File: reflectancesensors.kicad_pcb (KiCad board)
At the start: 2 copper layers, 42 x 29.5 mm, 10 parts, among them J1 Power, J2 Outputs, U1 TCRT5000L, U3 TCRT5000L

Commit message: some small changes
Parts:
- added H1: MountingHole, MountingHole:MountingHole_3.2mm_M3_DIN965, F.Cu at (79.0, 96.0)
- added H2: MountingHole, MountingHole:MountingHole_3.2mm_M3_DIN965, F.Cu at (79.0, 103.2)
- added H3: MountingHole, MountingHole:MountingHole_3.2mm_M3_DIN965, F.Cu at (79.0, 110.3)
- added H4: MountingHole, MountingHole:MountingHole_3.2mm_M3_DIN965, F.Cu at (79.0, 117.5)
- GND +3V3: renamed from J1
- Outputs 1,2: renamed from J2
- renumbered U3 to U1, U1 to U2
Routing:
- net GND: vias 90 -> 100
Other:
- board size 42 x 29.5 mm -> 48.5 x 35.5 mm

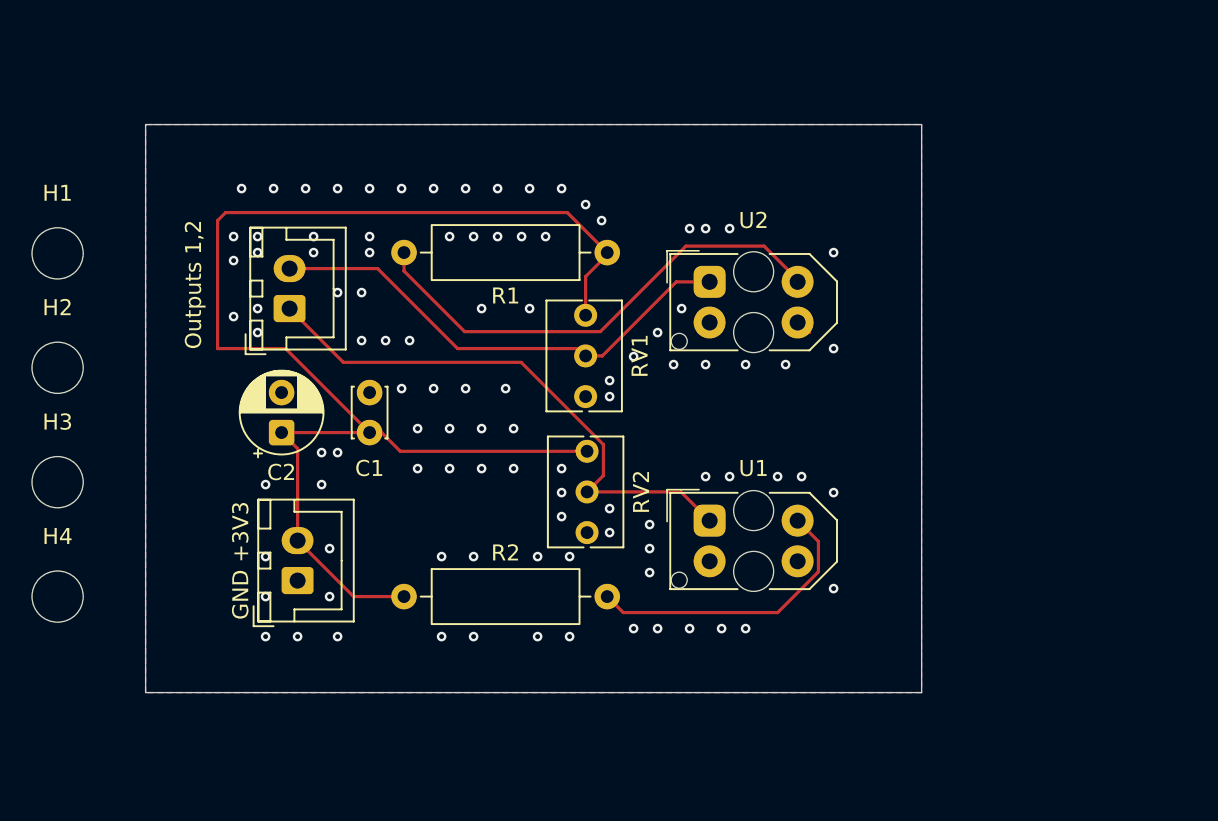
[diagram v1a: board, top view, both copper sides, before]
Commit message: adding high power reflectance
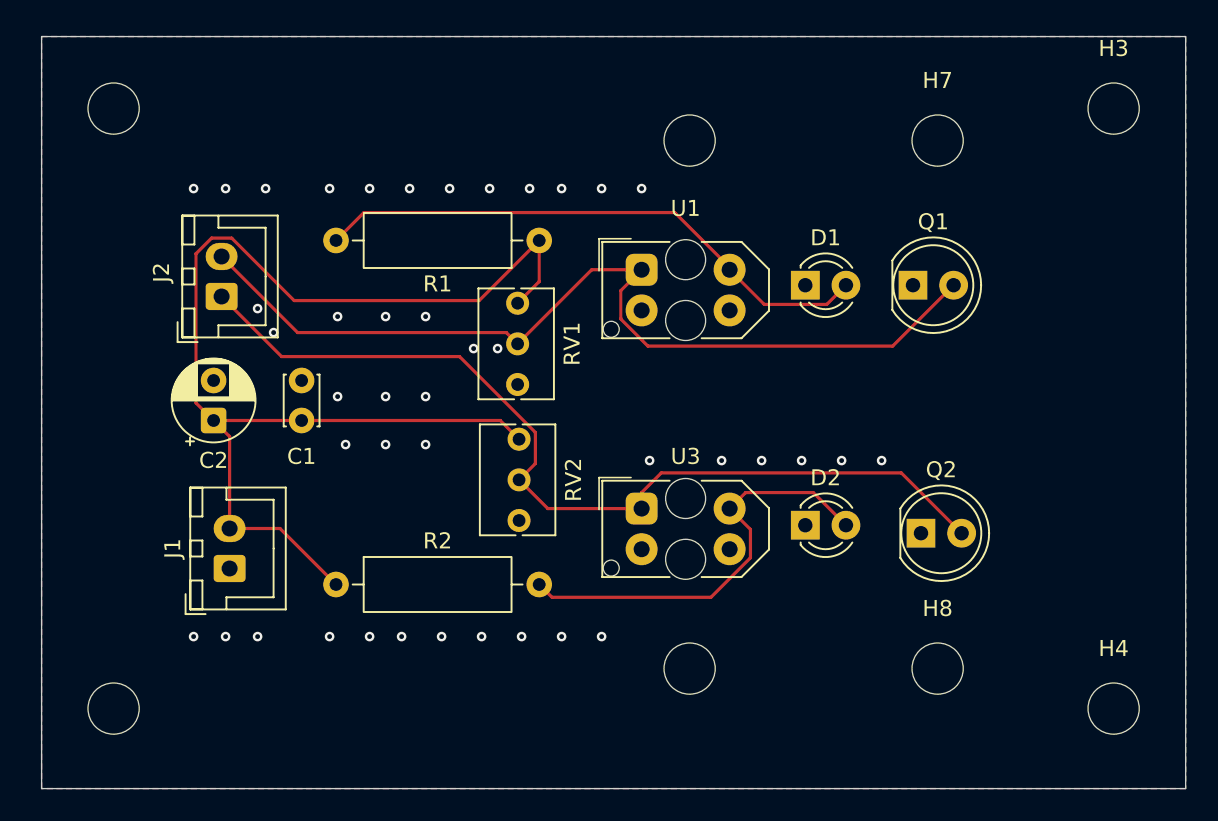
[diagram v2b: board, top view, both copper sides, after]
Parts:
- added D1: IR204A, LED_THT:LED_D3.0mm_IRBlack, F.Cu at (125.7, 98.0)
- added D2: IR204A, LED_THT:LED_D3.0mm_IRBlack, F.Cu at (125.7, 113.0)
- added H5: MountingHole, MountingHole:MountingHole_3.2mm_M3_DIN965, F.Cu at (118.5, 89.0)
- added H6: MountingHole, MountingHole:MountingHole_3.2mm_M3_DIN965, F.Cu at (118.5, 122.0)
- added H7: MountingHole, MountingHole:MountingHole_3.2mm_M3_DIN965, F.Cu at (134.0, 89.0)
- added H8: MountingHole, MountingHole:MountingHole_3.2mm_M3_DIN965, F.Cu at (134.0, 122.0)
- added Q1: BPW40, LED_THT:LED_D5.0mm_Clear, F.Cu at (132.5, 98.0)
- added Q2: BPW40, LED_THT:LED_D5.0mm_Clear, F.Cu at (133.0, 113.5)
- J1: renamed from GND +3V3
- J2: renamed from Outputs 1,2
- moved H3 70.0 mm to (145.0, 87.0)
- moved H4 66.4 mm to (145.0, 124.5)
- moved H2 21.6 mm to (82.5, 124.5)
- moved H1 9.70 mm to (82.5, 87.0)
- moved C1 4.32 mm to (94.2, 106.5)
- moved C2 4.32 mm to (88.8, 106.5)
- moved J1 4.32 mm to (89.8, 115.7)
- moved J2 4.32 mm to (89.2, 98.7)
- moved R1 4.32 mm to (109.1, 95.2)
- moved R2 4.32 mm to (96.4, 116.7)
- moved RV1 4.32 mm to (107.8, 104.2)
- moved RV2 4.32 mm to (107.8, 112.7)
- moved U1 4.32 mm to (115.5, 97.1)
- moved U3 4.32 mm to (115.5, 112.0)
- renumbered U2 to U1, U1 to U3
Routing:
- net Net-(J2-Pin_2): track 30.4 -> 57.1 mm
- net Net-(J2-Pin_1): track 34.9 -> 58.9 mm
- net +3V3: track 84.6 -> 75.9 mm
- net Net-(D2-A): track 18.4 -> 26.7 mm
- net Net-(D1-A): track 30.5 -> 35.6 mm
- net GND: track 1.01 -> 0.00 mm, vias 100 -> 0
- net unconnected-(RV1-Pad1): track 0.50 -> 0.00 mm
- net (no net): vias 0 -> 42
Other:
- board size 48.5 x 35.5 mm -> 71.5 x 47 mm

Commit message: small changes
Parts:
- removed H1, H2, H3, H4: MountingHole, MountingHole:MountingHole_3.2mm_M3_DIN965
- D1, D2: footprint LED_THT:LED_D3.0mm_IRBlack -> LED_THT:LED_D5.0mm
- moved H7 62.5 mm to (82.5, 124.5)
- moved H6 43.9 mm to (145.0, 87.0)
- moved H5 36.1 mm to (82.5, 87.0)
- moved H8 11.3 mm to (145.0, 124.5)
- moved Q1 2.54 mm to (135.0, 98.0), turned to 180 degrees
- moved Q2 2.54 mm to (135.5, 113.5), turned to 180 degrees
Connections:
- Q1 pad 1: GND -> Net-(J2-Pin_2)
- Q1 pad 2: Net-(J2-Pin_2) -> GND
- Q2 pad 1: GND -> Net-(J2-Pin_1)
- Q2 pad 2: Net-(J2-Pin_1) -> GND
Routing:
- net Net-(J2-Pin_2): track 57.1 -> 65.0 mm
- net GND: vias 0 -> 83
- net (no net): vias 42 -> 0

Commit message: changing connector
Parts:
- removed J1: Power, Connector_JST:JST_XH_B2B-XH-A_1x02_P2.50mm_Vertical
- J2: value Outputs -> Conn_01x04_Socket; footprint Connector_JST:JST_XH_B2B-XH-A_1x02_P2.50mm_Vertical -> Connector_JST:JST_XH_S4B-XH-A-1_1x04_P2.50mm_Horizontal
- moved C2 15.0 mm to (103.5, 109.0), turned to -90 degrees
- moved C1 9.17 mm to (103.0, 103.8)
- moved D1 5.25 mm to (131.0, 98.5)
- moved D2 5.25 mm to (131.0, 113.5)
- moved R1 5.25 mm to (114.3, 95.7)
- moved RV1 5.25 mm to (113.0, 104.7)
- moved U1 5.25 mm to (120.7, 97.5)
- moved U3 5.25 mm to (120.7, 112.5)
- moved Q1 5.25 mm to (140.2, 98.5)
- moved Q2 5.25 mm to (140.7, 114.0)
- moved R2 5.25 mm to (101.6, 117.2)
- moved RV2 5.25 mm to (113.1, 113.2)
- moved J2 5.06 mm to (92.3, 102.8), turned to -90 degrees
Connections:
- J2 pad 1: Net-(J2-Pin_1) -> +3V3
- Q2 pad 1: Net-(J2-Pin_1) -> Net-(J2-Pin_3)
- RV2 pad 2: Net-(J2-Pin_1) -> Net-(J2-Pin_3)
- U3 pad 1: Net-(J2-Pin_1) -> Net-(J2-Pin_3)
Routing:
- net Net-(J2-Pin_3): track 0.00 -> 61.8 mm
- net Net-(J2-Pin_1): track 58.9 -> 0.00 mm
- net +3V3: track 75.9 -> 34.9 mm
- net Net-(J2-Pin_2): track 65.0 -> 67.5 mm
- net GND: vias 83 -> 79

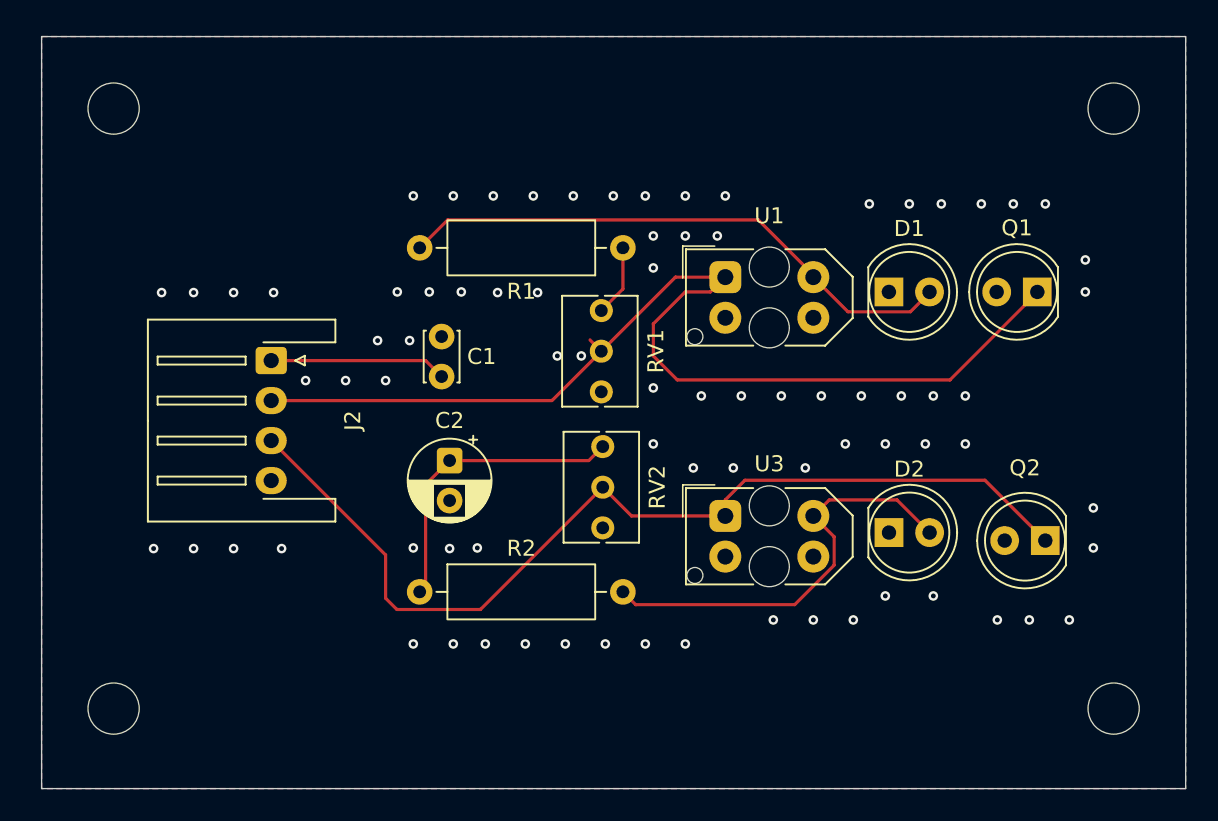
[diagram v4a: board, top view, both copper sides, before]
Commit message: adding labels and editing traces
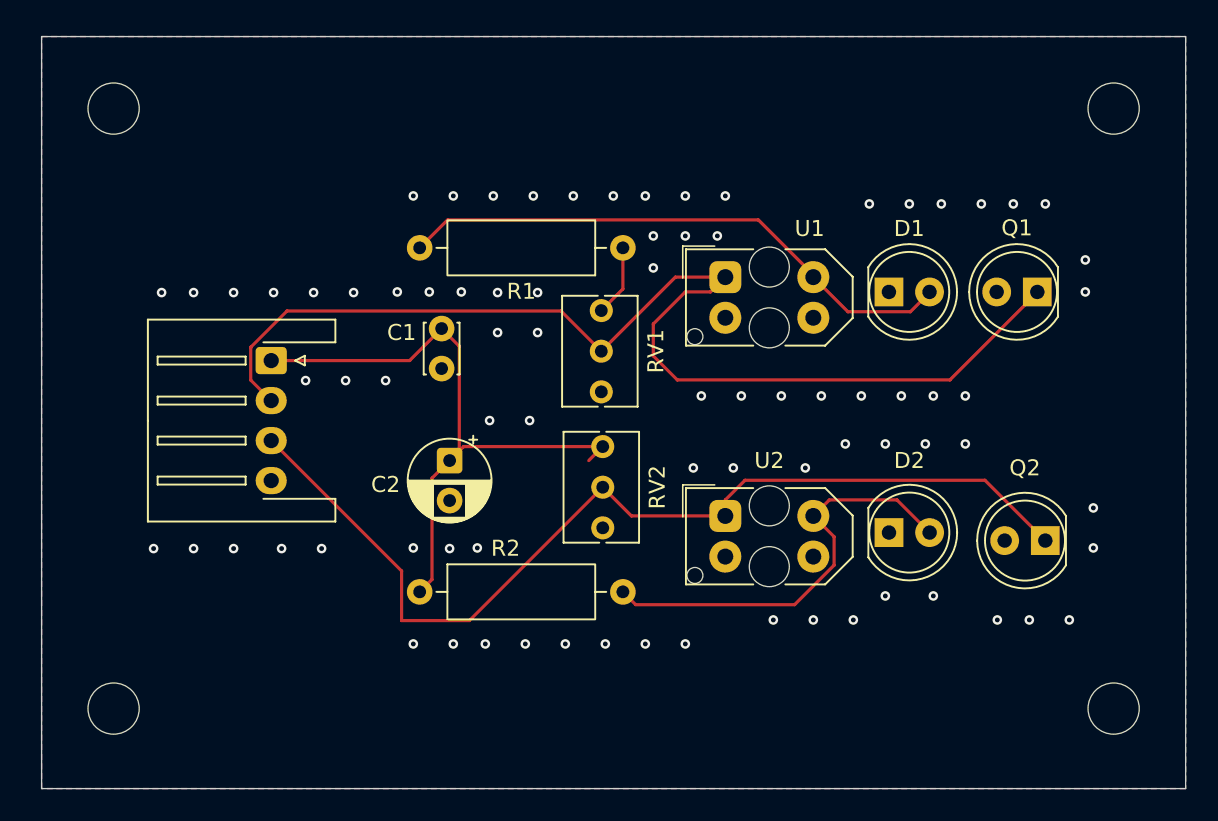
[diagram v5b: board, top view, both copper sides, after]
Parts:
- moved C1 3.00 mm to (103.0, 100.8), turned to -90 degrees
- renumbered U3 to U2
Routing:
- net +3V3: track 34.9 -> 45.5 mm
- net Net-(J2-Pin_2): track 67.5 -> 72.0 mm
- net GND: vias 79 -> 80

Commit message: final touches
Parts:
- moved C2 15.6 mm to (90.4, 117.5), turned to 90 degrees
- moved C1 15.2 mm to (89.9, 93.0)
- moved RV2 7.62 mm to (108.1, 107.5), turned to 90 degrees
- moved D1 4.75 mm to (126.2, 98.0)
- moved D2 4.75 mm to (126.2, 113.0)
- moved R1 4.75 mm to (109.6, 95.2)
- moved RV1 4.75 mm to (108.2, 104.2)
- moved U1 4.75 mm to (116.0, 97.1)
- moved U2 4.75 mm to (116.0, 112.0)
- moved Q1 4.75 mm to (135.5, 98.0)
- moved Q2 4.75 mm to (136.0, 113.5)
- moved R2 4.75 mm to (96.9, 116.7)
- moved J2 3.01 mm to (95.3, 102.0)
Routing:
- net +3V3: track 45.5 -> 66.4 mm
- net Net-(J2-Pin_3): track 62.1 -> 45.9 mm
- net Net-(J2-Pin_2): track 72.0 -> 58.4 mm
- net GND: vias 80 -> 71

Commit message: fixing multiple versions
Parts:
- added REF**: , GS_Virtual:ENPH253_Logo_Small, F.Cu at (99.2, 124.7)
- moved C1 19.3 mm to (106.0, 103.6), turned to 90 degrees
- moved C2 18.3 mm to (106.5, 108.9), turned to -90 degrees
- moved RV2 9.79 mm to (116.1, 113.1), turned to -90 degrees
- moved H5 9.50 mm to (92.0, 87.0)
- moved H7 9.50 mm to (92.0, 124.5)
- moved D1 7.76 mm to (134.0, 98.3)
- moved Q1 7.76 mm to (143.2, 98.3)
- moved Q2 7.76 mm to (143.8, 113.9)
- moved R1 7.76 mm to (117.3, 95.6)
- moved R2 7.76 mm to (104.7, 117.1)
- moved RV1 7.76 mm to (116.0, 104.6)
- moved U1 7.76 mm to (123.8, 97.4)
- moved U3 7.76 mm to (123.8, 112.3)
- moved D2 7.76 mm to (134.0, 113.4)
- moved J2 0.59 mm to (95.4, 102.6)
- renumbered U2 to U3
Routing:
- net +3V3: track 66.4 -> 34.9 mm
- net Net-(J2-Pin_3): track 45.9 -> 61.8 mm
- net Net-(J2-Pin_2): track 58.4 -> 67.5 mm
- net GND: vias 71 -> 79
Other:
- board size 71.5 x 47 mm -> 62 x 47 mm
- board text added: "Line following"
